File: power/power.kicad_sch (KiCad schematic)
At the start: 18 parts, among them J1 GPIO, J18 JP_VCC_PWM, J19 Conn_01x01, J2 PWM_OUT, J20 CONN_RS485, J3 PWM_IN, J4 JP_EXT, J5 JP_VOLTS, J8 PWM_OUT, J9 JP_VCC_PWM, Q1 D15P05

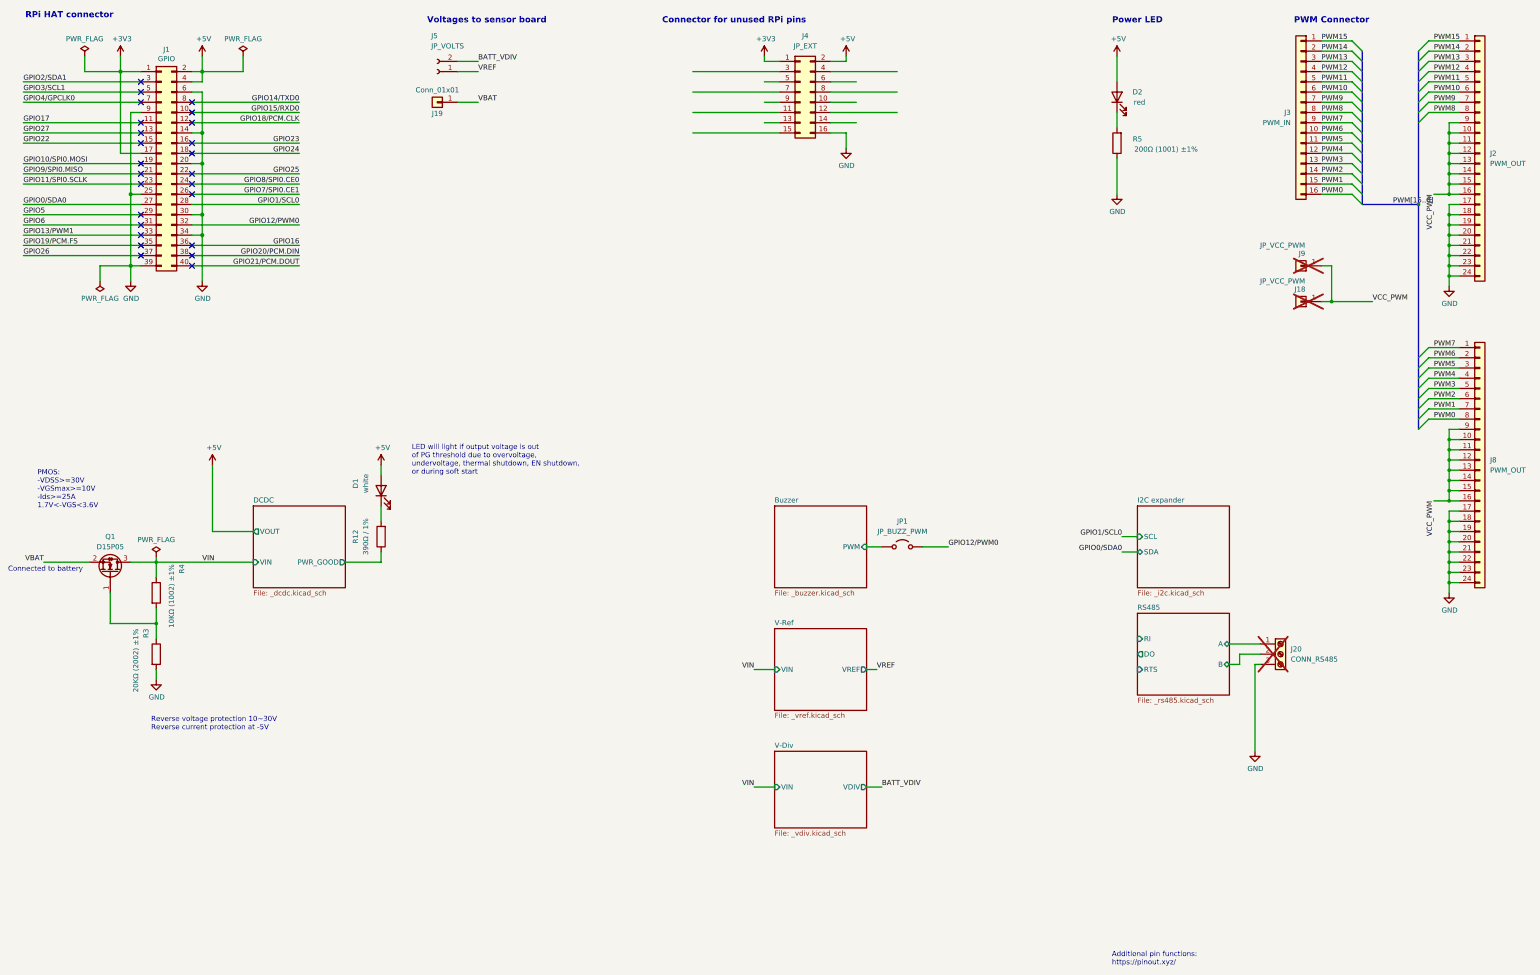
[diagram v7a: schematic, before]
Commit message: add 100nF to SP3485
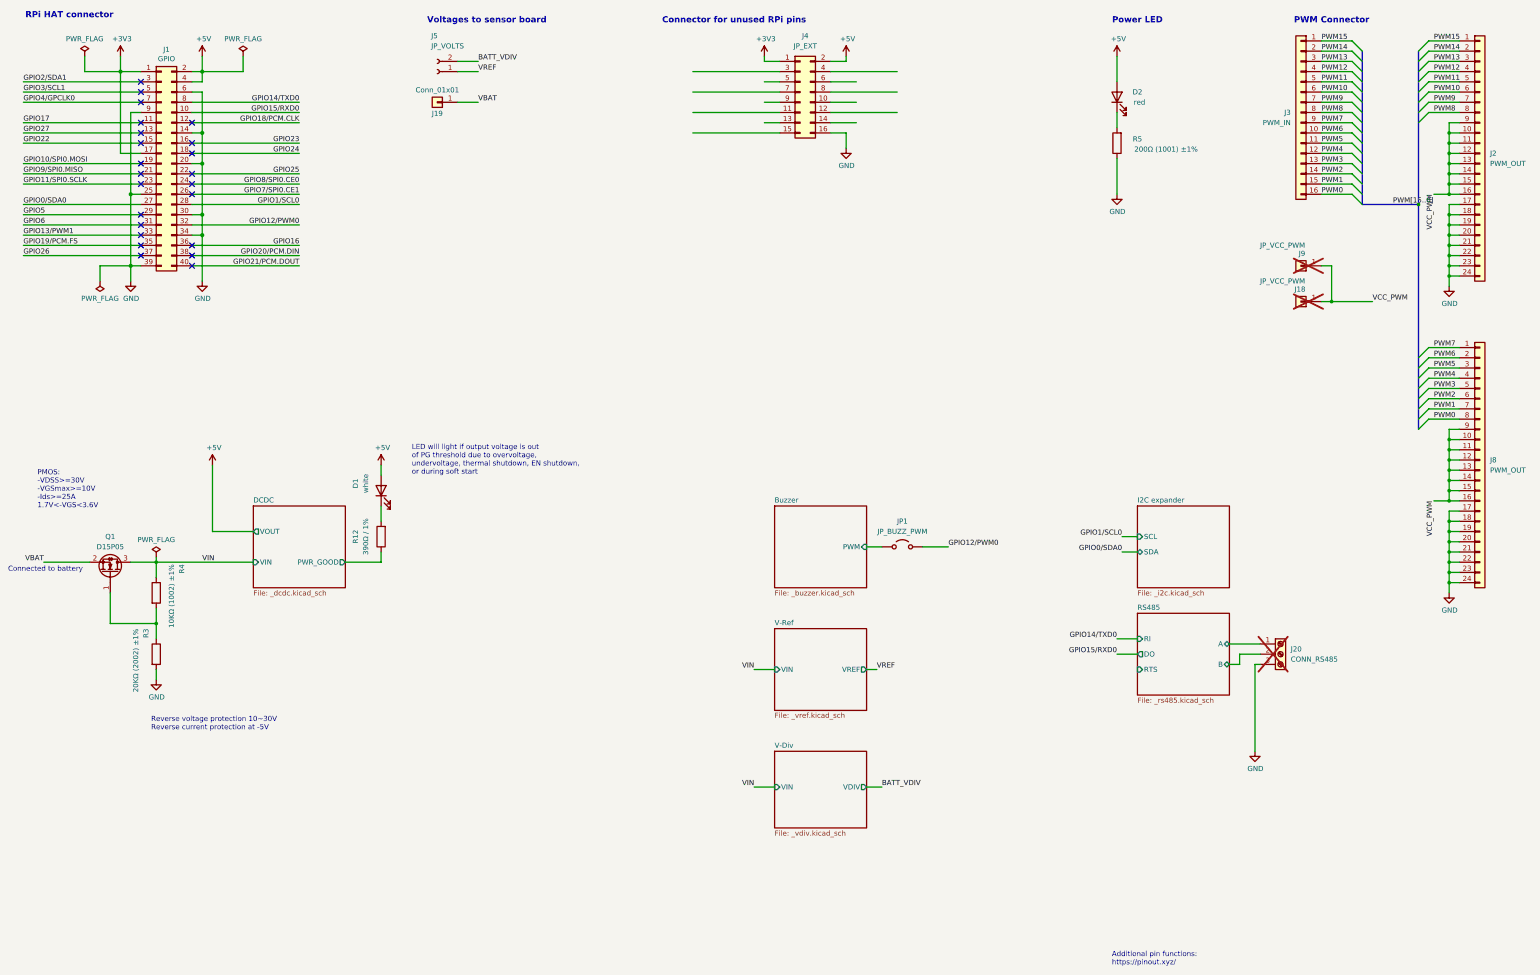
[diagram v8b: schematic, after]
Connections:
- no-connect marks 25 -> 23
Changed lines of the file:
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@@
-	)
-	(no_connect
-		(at 73.66 44.45)
 	)
 	(no_connect
@@
 	)
 	(no_connect
-		(at 73.66 46.99)
-	)
-	(no_connect
 		(at 60.96 59.69)
 	)
@@
 	(wire
 		(pts
+			(xy 303.53 177.8) (xy 308.61 177.8)
+		)
+		(stroke
+			(width 0)
+			(type default)
+		)
+	)
+	(wire
+		(pts
 			(xy 386.08 69.85) (xy 388.62 69.85)
 		)
@@
 			(width 0)
 			(type solid)
+		)
+	)
+	(wire
+		(pts
+			(xy 303.53 181.61) (xy 308.61 181.61)
+		)
+		(stroke
+			(width 0)
+			(type default)
 		)
 	)
@@
 		)
 	)
+	(label "GPIO15{slash}RXD0"
+		(at 303.53 181.61 180)
+		(effects
+			(font
+				(size 1.27 1.27)
+			)
+			(justify right bottom)
+		)
+	)
 	(label "PWM11"
 		(at 354.33 39.37 0)
@@
 		)
 	)
+	(label "GPIO14{slash}TXD0"
+		(at 303.53 177.8 180)
+		(effects
+			(font
+				(size 1.27 1.27)
+			)
+			(justify right bottom)
+		)
+	)
